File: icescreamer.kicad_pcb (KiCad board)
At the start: 2 copper layers, 46 parts, among them CON1 BARREL_JACK, J1 JACK_3P, J2 JACK_3P, P1 CONN_2, Q1 NPN, Q2 NPN, SW1 3PDT, U1 TL072, U2 TLE2426NR

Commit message: Add outline
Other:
- board outline added: 48 x 98 mm
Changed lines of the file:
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@@
     )
   )
+  (gr_line (start -19.000000 -49.000000) (end 19.000000 -49.000000) (angle 90) (layer Edge.Cuts) (width 0.200000))
+  (gr_line (start 24.000000 -44.000000) (end 24.000000 44.000000) (angle 90) (layer Edge.Cuts) (width 0.200000))
+  (gr_line (start 19.000000 49.000000) (end -19.000000 49.000000) (angle 90) (layer Edge.Cuts) (width 0.200000))
+  (gr_line (start -24.000000 44.000000) (end -24.000000 -44.000000) (angle 90) (layer Edge.Cuts) (width 0.200000))
+  (gr_arc (start 19.000000 -44.000000) (end 19.000000 -49.000000) (angle 90) (layer Edge.Cuts) (width 0.200000))
+  (gr_arc (start 19.000000 44.000000) (end 24.000000 44.000000) (angle 90) (layer Edge.Cuts) (width 0.200000))
+  (gr_arc (start -19.000000 44.000000) (end -19.000000 49.000000) (angle 90) (layer Edge.Cuts) (width 0.200000))
+  (gr_arc (start -19.000000 -44.000000) (end -24.000000 -44.000000) (angle 90) (layer Edge.Cuts) (width 0.200000))
 )

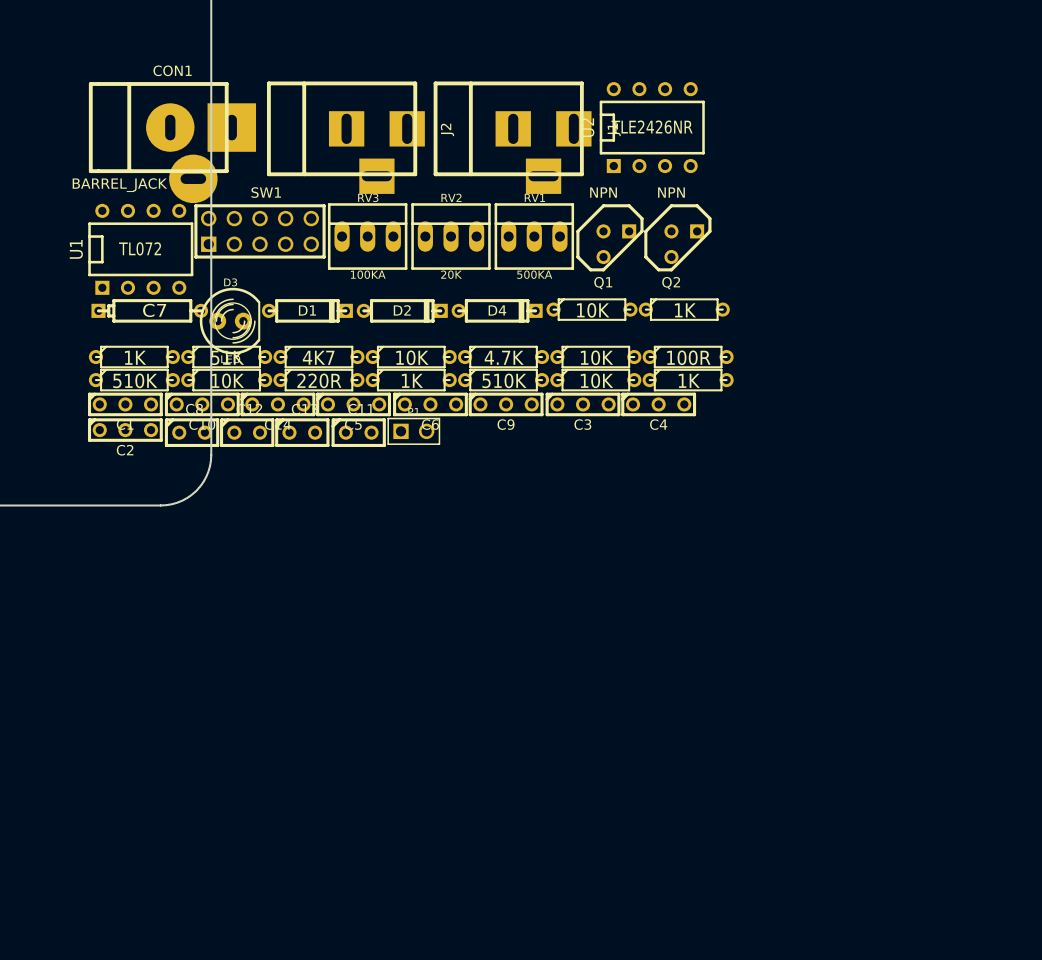
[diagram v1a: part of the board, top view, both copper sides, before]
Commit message: Add components to pcb file, add temp component to this main repo as backup
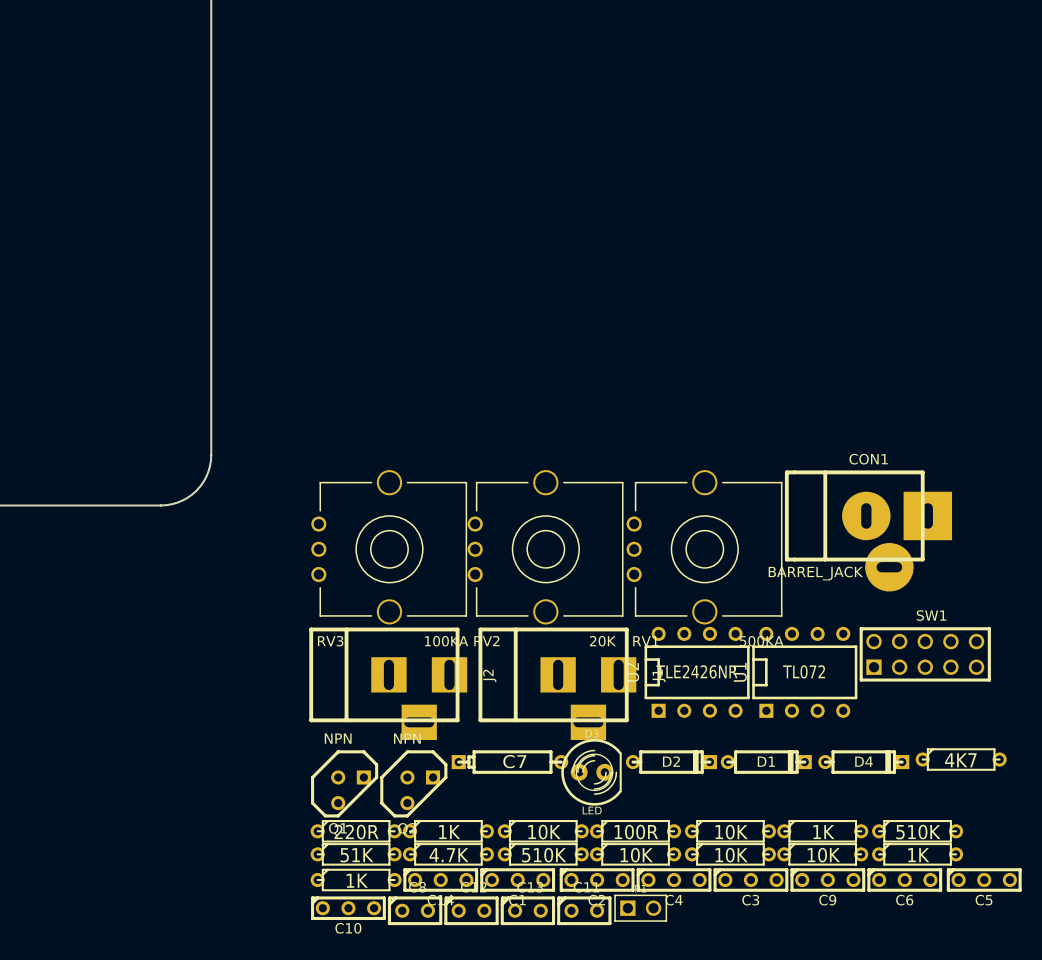
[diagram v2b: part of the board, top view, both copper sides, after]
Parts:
- RV1, RV2, RV3: footprint PINHEAD1-3 -> Passive_pot_THD
- moved CON1 79.0 mm to (88.9, 50.0)
- moved C5 78.3 mm to (100.6, 86.1)
- moved SW1 78.1 mm to (94.7, 63.8)
- moved U1 78.0 mm to (82.8, 65.5)
- moved R11 75.1 mm to (98.3, 74.2)
- moved C6 66.5 mm to (92.7, 86.1)
- moved R7 65.2 mm to (38.4, 86.1)
- moved C2 64.6 mm to (62.2, 86.1)
- moved R8 64.0 mm to (84.6, 83.6)
- moved D1 63.8 mm to (79.0, 74.4)
- moved R2 62.0 mm to (56.9, 83.6)
- moved R3 62.0 mm to (66.0, 83.6)
- moved C1 61.1 mm to (54.4, 86.1)
- moved R13 60.7 mm to (94.0, 81.3)
- moved R10 60.5 mm to (84.6, 81.3)
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
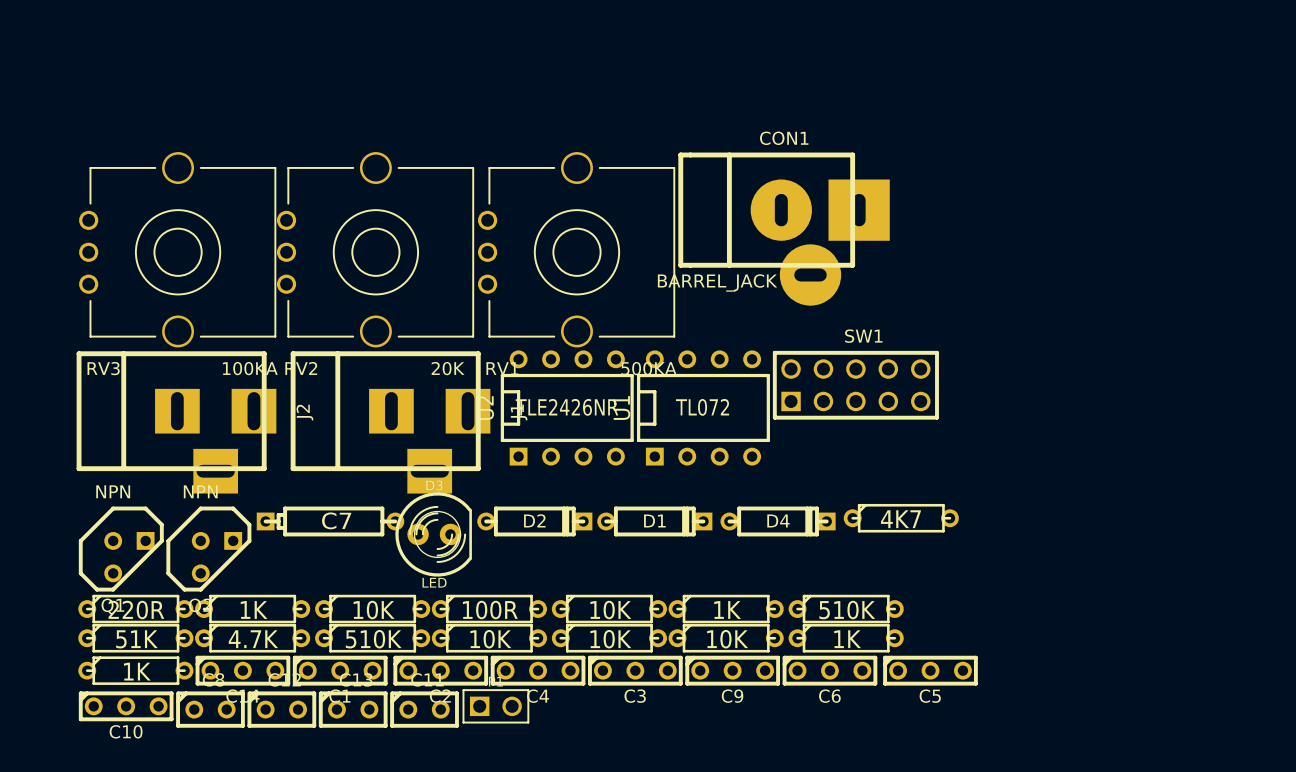
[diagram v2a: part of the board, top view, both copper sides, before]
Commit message: Update footprint for female jack in netlist
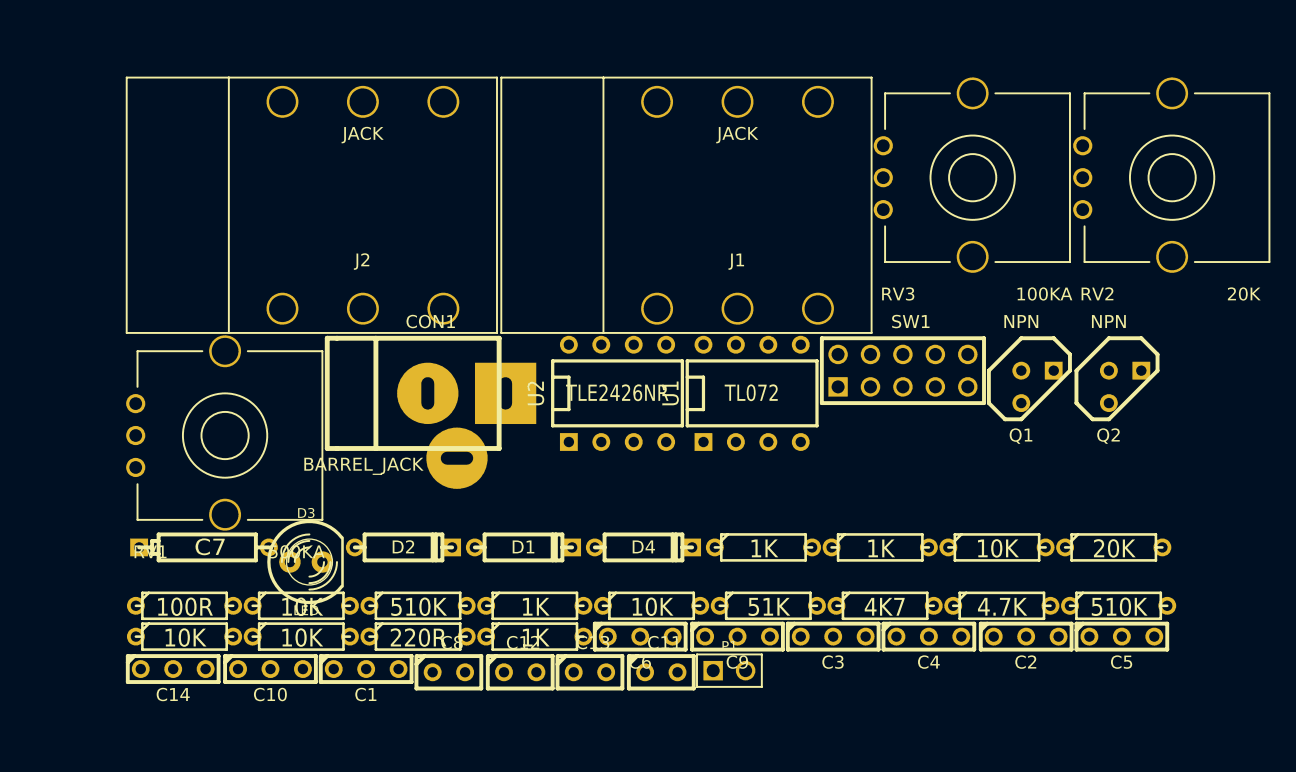
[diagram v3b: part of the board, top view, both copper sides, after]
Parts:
- added R17: 20K, R3, F.Cu at (114.9, 76.5)
- J1, J2: value JACK_3P -> JACK; footprint BARREL_JACK -> Conn_Jack_Female_635_THD
- moved Q1 72.4 mm to (109.0, 63.9)
- moved Q2 72.4 mm to (115.8, 63.9)
- moved RV2 62.6 mm to (119.5, 47.5)
- moved RV3 62.5 mm to (103.9, 47.5)
- moved R5 58.7 mm to (106.2, 81.0)
- moved R2 58.5 mm to (115.3, 81.0)
- moved R7 50.1 mm to (87.5, 76.5)
- moved R6 49.6 mm to (87.9, 81.0)
- moved R1 49.4 mm to (96.6, 76.5)
- moved R16 49.1 mm to (105.8, 76.5)
- moved C2 45.9 mm to (108.1, 83.4)
- moved R13 33.5 mm to (60.5, 81.0)
- moved J1 31.7 mm to (85.5, 49.7)
- moved CON1 31.2 mm to (61.2, 64.4)
- moved RV1 31.1 mm to (45.3, 67.7)
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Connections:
- CON1 pad 1: N-0000025 -> N-0000018
- J1 pad 1: N-0000037 -> (no net)
- J1 pad 2: -5V -> (no net)
- J1 pad 3: N-0000025 -> (no net)
- J2 pad 1: N-0000036 -> (no net)
- P1 pad 2: N-0000025 -> N-0000018
- SW1 pad 1: N-0000036 -> N-0000033
- SW1 pad 5: N-0000037 -> N-0000028
- SW1 pad 8: N-0000036 -> N-0000033

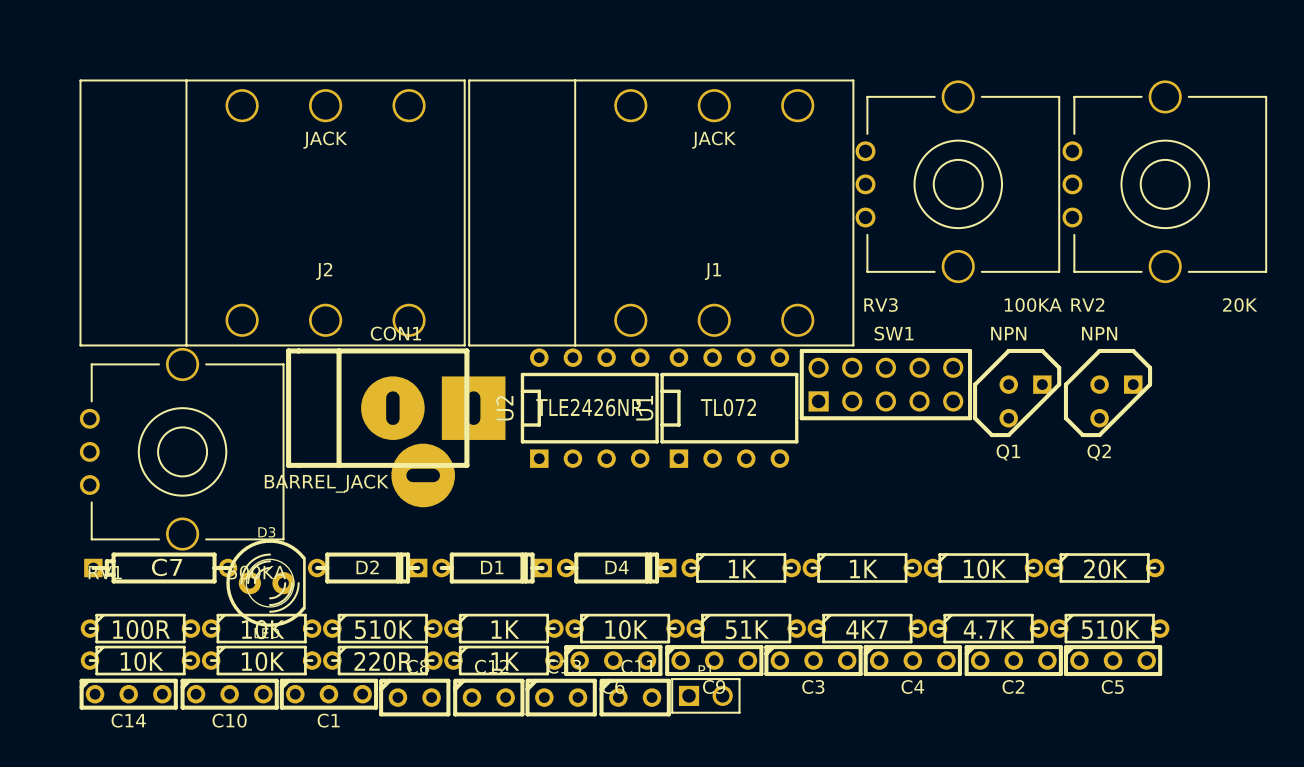
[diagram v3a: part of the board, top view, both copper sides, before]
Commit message: Update female jack pinout
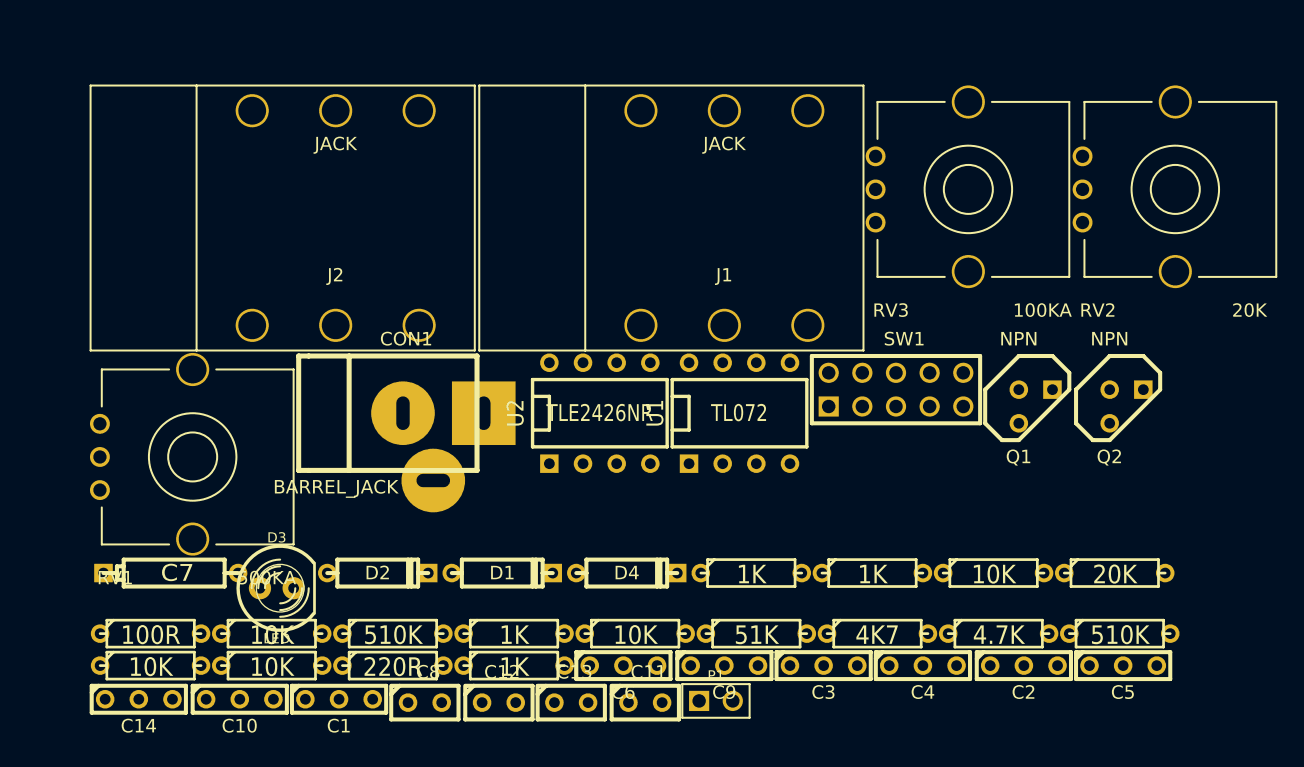
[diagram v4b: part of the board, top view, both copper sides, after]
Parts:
- moved C1 0.85 mm to (57.1, 86.4)
- moved C11 0.85 mm to (80.3, 86.6)
- moved C12 0.85 mm to (69.2, 86.6)
- moved C13 0.85 mm to (74.7, 86.6)
- moved C14 0.85 mm to (42.0, 86.4)
- moved C2 0.85 mm to (108.8, 83.8)
- moved C3 0.85 mm to (93.7, 83.8)
- moved C4 0.85 mm to (101.2, 83.8)
- moved C5 0.85 mm to (116.3, 83.8)
- moved C6 0.85 mm to (78.6, 83.8)
- moved C7 0.85 mm to (44.5, 76.8)
- moved C8 0.85 mm to (63.6, 86.6)
- moved C9 0.85 mm to (86.2, 83.8)
- moved CON1 0.85 mm to (62.0, 64.8)
- moved D1 0.85 mm to (69.5, 76.8)
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
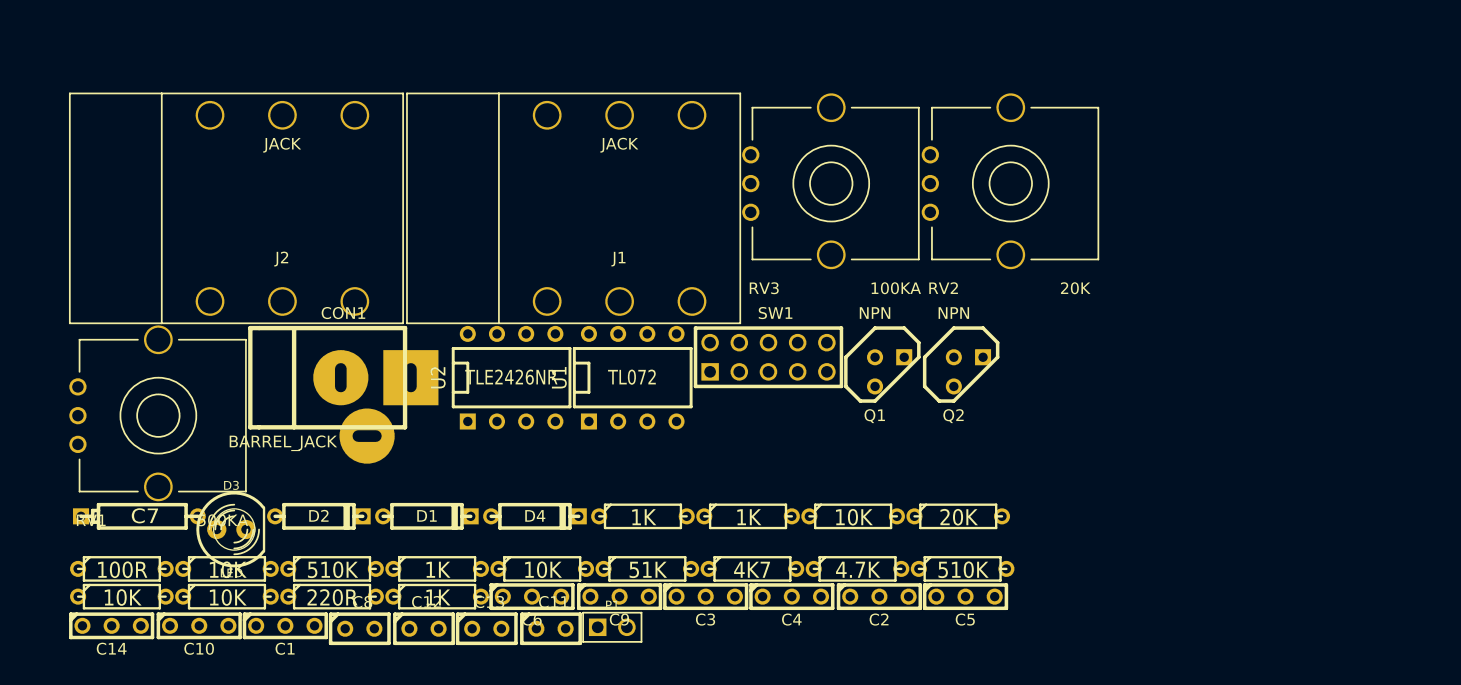
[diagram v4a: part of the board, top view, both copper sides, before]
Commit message: Add new footprints
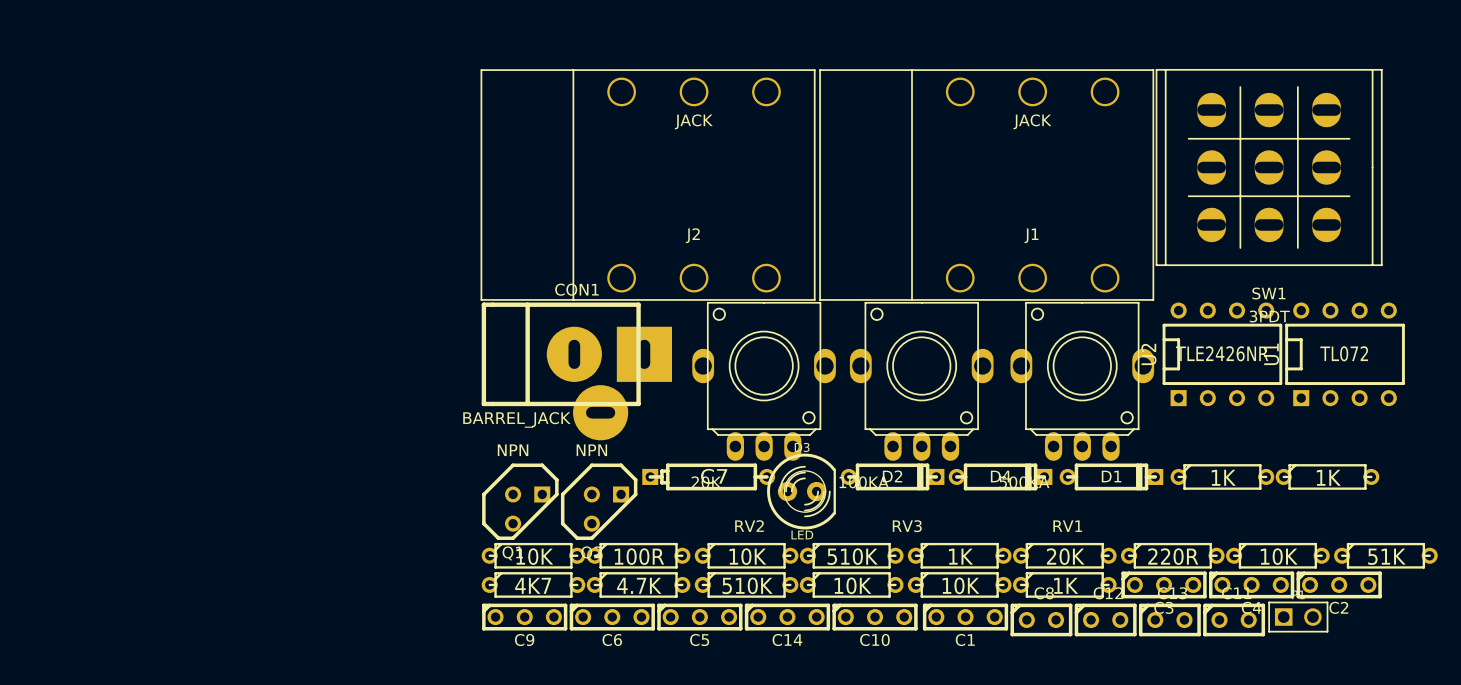
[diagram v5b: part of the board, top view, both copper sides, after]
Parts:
- RV1, RV2, RV3: footprint Passive_pot_THD -> Passives_BOURNS_PTV09A
- SW1: footprint PIN_ARRAY_5x2 -> Switches_Stomp_3PDT
- moved RV1 80.5 mm to (126.5, 63.8)
- moved R9 73.2 mm to (134.4, 80.3)
- moved R6 64.3 mm to (152.9, 80.3)
- moved R8 64.0 mm to (143.5, 80.3)
- moved R4 63.8 mm to (115.8, 82.8)
- moved R3 63.5 mm to (106.4, 82.8)
- moved U1 62.0 mm to (149.4, 62.7)
- moved U2 61.9 mm to (138.7, 62.7)
- moved P1 59.7 mm to (145.3, 85.6)
- moved D1 59.7 mm to (129.0, 73.4)
- moved C11 59.4 mm to (139.7, 85.9)
- moved C13 59.4 mm to (134.1, 85.9)
- moved C8 59.3 mm to (122.9, 85.9)
- moved C12 59.3 mm to (128.5, 85.9)
- moved C1 59.2 mm to (116.3, 85.6)
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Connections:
- C5 pad 1: N-0000016 (its old number) -> N-0000018
- R10 pad 1: N-0000011 (its old number) -> N-0000017
- R7 pad 2: N-0000016 (its old number) -> N-0000018
- R8 pad 2: N-0000016 (its old number) -> N-0000018
- RV2 pad 1: N-0000016 (its old number) -> N-0000017
- RV2 pad 3: N-0000011 (its old number) -> N-0000018
- U1 pad 5: N-0000016 (its old number) -> N-0000018
- U1 pad 6: N-0000011 (its old number) -> N-0000017
